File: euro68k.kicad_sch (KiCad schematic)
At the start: 5 parts, among them U1 68000D, U2 AS6C4008-55PCN, U3 28C256, U4 AS6C4008-55PCN, U5 28C256

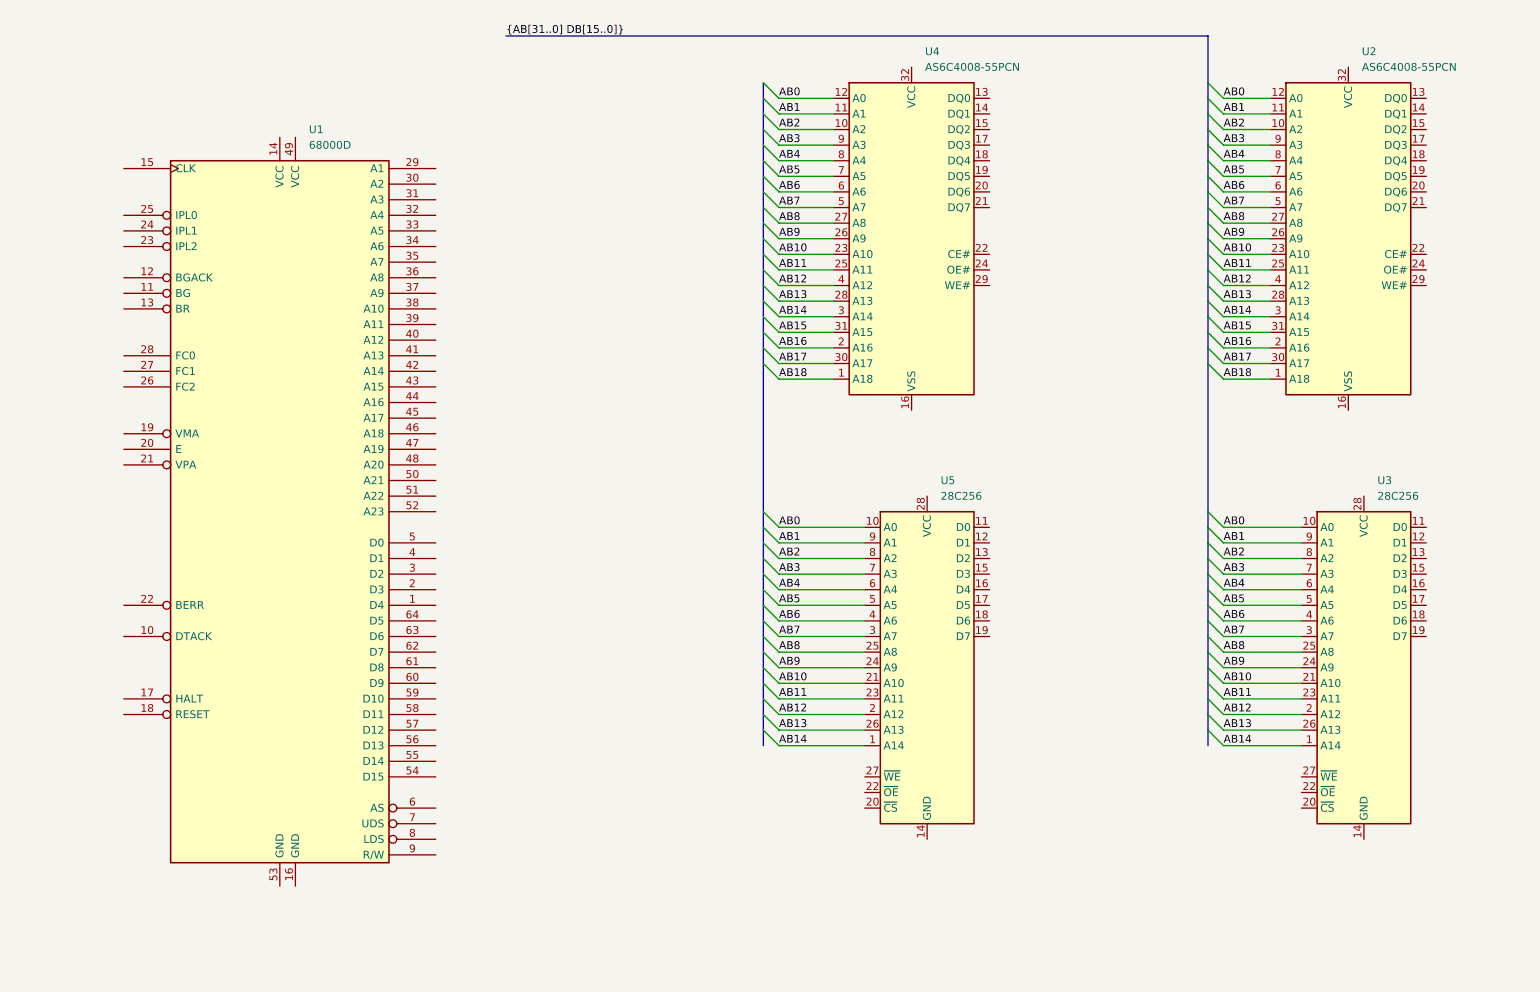
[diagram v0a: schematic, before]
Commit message: databuss til minne
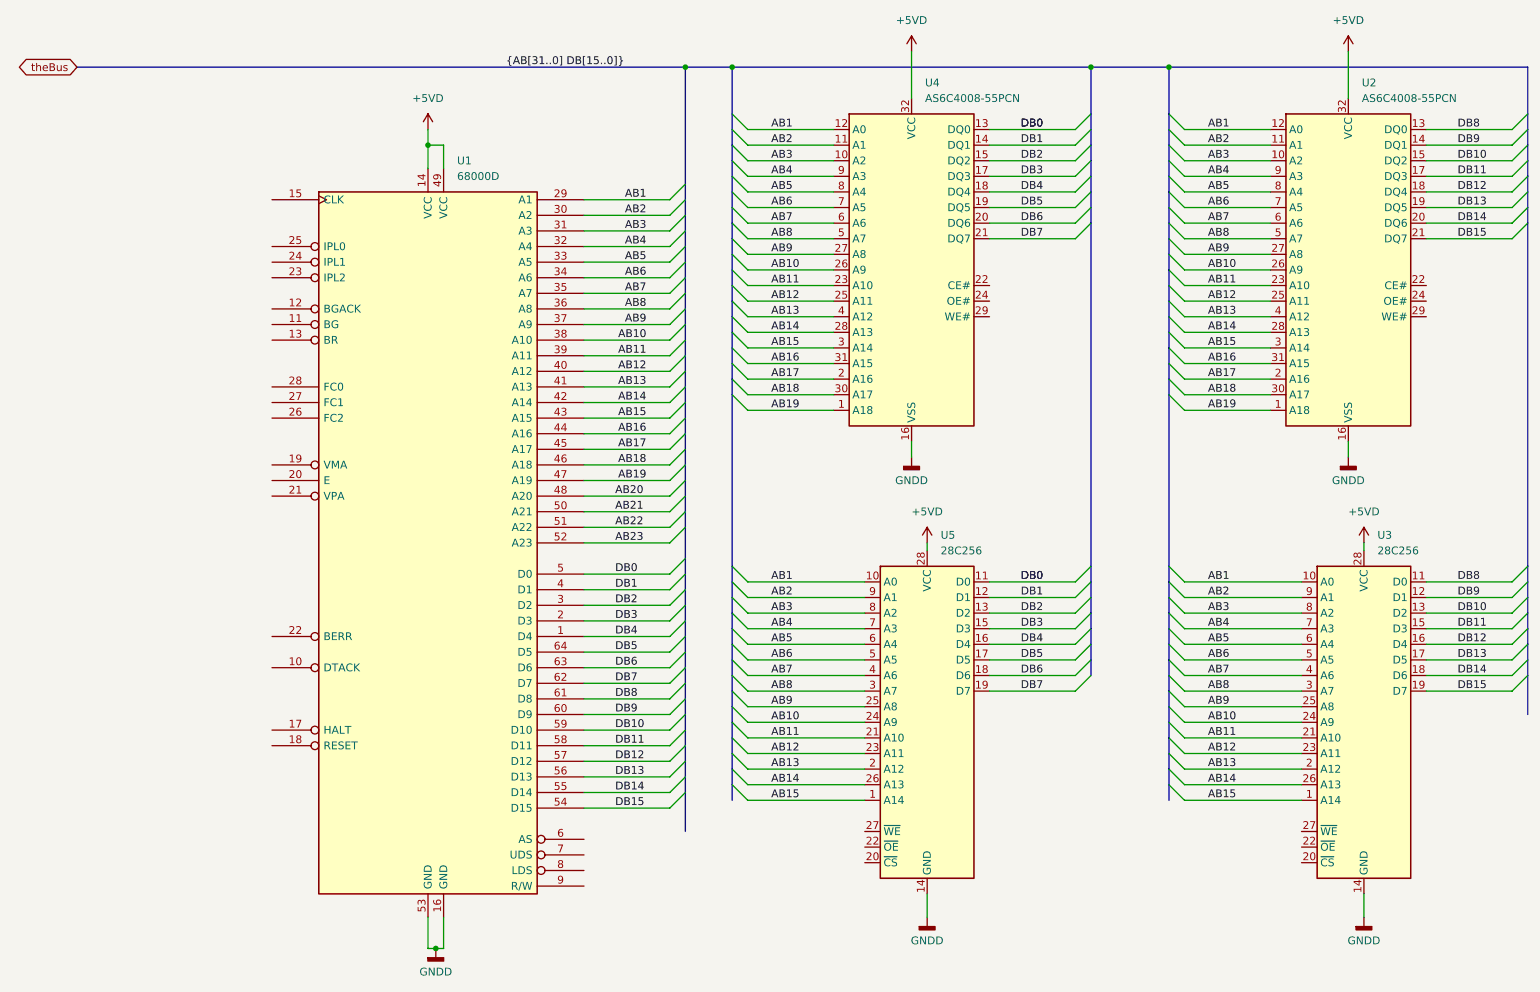
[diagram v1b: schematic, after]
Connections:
- net AB0 is gone; now on net AB1: U2.12 (A0), U3.10 (A0), U4.12 (A0), U5.10 (A0)
- net AB1: now also U1.29 (A1); no longer U2.11 (A1), U3.9 (A1), U4.11 (A1), U5.9 (A1)
- net AB10: now also U1.38 (A10), U2.26 (A9), U3.24 (A9), U4.26 (A9), U5.24 (A9); no longer U2.23 (A10), U3.21 (A10), U4.23 (A10), U5.21 (A10)
- net AB11: now also U1.39 (A11), U2.23 (A10), U3.21 (A10), U4.23 (A10), U5.21 (A10); no longer U2.25 (A11), U3.23 (A11), U4.25 (A11), U5.23 (A11)
- net AB12: now also U1.40 (A12), U2.25 (A11), U3.23 (A11), U4.25 (A11), U5.23 (A11); no longer U2.4 (A12), U3.2 (A12), U4.4 (A12), U5.2 (A12)
- net AB13: now also U1.41 (A13), U2.4 (A12), U3.2 (A12), U4.4 (A12), U5.2 (A12); no longer U2.28 (A13), U3.26 (A13), U4.28 (A13), U5.26 (A13)
- net AB14: now also U1.42 (A14), U2.28 (A13), U3.26 (A13), U4.28 (A13), U5.26 (A13); no longer U2.3 (A14), U3.1 (A14), U4.3 (A14), U5.1 (A14)
- net AB15: now also U1.43 (A15), U2.3 (A14), U3.1 (A14), U4.3 (A14), U5.1 (A14); no longer U2.31 (A15), U4.31 (A15)
- net AB16: now also U1.44 (A16), U2.31 (A15), U4.31 (A15); no longer U2.2 (A16), U4.2 (A16)
- net AB17: now also U1.45 (A17), U2.2 (A16), U4.2 (A16); no longer U2.30 (A17), U4.30 (A17)
- net AB18: now also U1.46 (A18), U2.30 (A17), U4.30 (A17); no longer U2.1 (A18), U4.1 (A18)
- net AB2: now also U1.30 (A2), U2.11 (A1), U3.9 (A1), U4.11 (A1), U5.9 (A1); no longer U2.10 (A2), U3.8 (A2), U4.10 (A2), U5.8 (A2)
- net AB3: now also U1.31 (A3), U2.10 (A2), U3.8 (A2), U4.10 (A2), U5.8 (A2); no longer U2.9 (A3), U3.7 (A3), U4.9 (A3), U5.7 (A3)
- net AB4: now also U1.32 (A4), U2.9 (A3), U3.7 (A3), U4.9 (A3), U5.7 (A3); no longer U2.8 (A4), U3.6 (A4), U4.8 (A4), U5.6 (A4)
- net AB5: now also U1.33 (A5), U2.8 (A4), U3.6 (A4), U4.8 (A4), U5.6 (A4); no longer U2.7 (A5), U3.5 (A5), U4.7 (A5), U5.5 (A5)
- net AB6: now also U1.34 (A6), U2.7 (A5), U3.5 (A5), U4.7 (A5), U5.5 (A5); no longer U2.6 (A6), U3.4 (A6), U4.6 (A6), U5.4 (A6)
- net AB7: now also U1.35 (A7), U2.6 (A6), U3.4 (A6), U4.6 (A6), U5.4 (A6); no longer U2.5 (A7), U3.3 (A7), U4.5 (A7), U5.3 (A7)
- net AB8: now also U1.36 (A8), U2.5 (A7), U3.3 (A7), U4.5 (A7), U5.3 (A7); no longer U2.27 (A8), U3.25 (A8), U4.27 (A8), U5.25 (A8)
- net AB9: now also U1.37 (A9), U2.27 (A8), U3.25 (A8), U4.27 (A8), U5.25 (A8); no longer U2.26 (A9), U3.24 (A9), U4.26 (A9), U5.24 (A9)
- net DB4: now reaches U1.1 (D4)
- net DB4: now also U4.18 (DQ4), U5.16 (D4)
- net +5VD: now reaches U1.14 (VCC)
- net +5VD: now also U1.49 (VCC), U2.32 (VCC), U3.28 (VCC), U4.32 (VCC), U5.28 (VCC)
- net GNDD: now reaches U1.16 (GND)
- net GNDD: now also U1.53 (GND), U2.16 (VSS), U3.14 (GND), U4.16 (VSS), U5.14 (GND)
- net DB3: now reaches U1.2 (D3)
- net DB3: now also U4.17 (DQ3), U5.15 (D3)
- net DB2: now reaches U1.3 (D2)
- net DB2: now also U4.15 (DQ2), U5.13 (D2)
- net DB1: now reaches U1.4 (D1)
- net DB1: now also U4.14 (DQ1), U5.12 (D1)
- net AB19: now reaches U1.47 (A19)
- net AB19: now also U2.1 (A18), U4.1 (A18)
- net AB20: now reaches U1.48 (A20)
- net DB0: now reaches U1.5 (D0)
- net DB0: now also U4.13 (DQ0), U5.11 (D0)
- net AB21: now reaches U1.50 (A21)
- net AB22: now reaches U1.51 (A22)
- net AB23: now reaches U1.52 (A23)
- net DB15: now reaches U1.54 (D15)
- net DB15: now also U2.21 (DQ7), U3.19 (D7)
- net DB14: now reaches U1.55 (D14)
- net DB14: now also U2.20 (DQ6), U3.18 (D6)
- net DB13: now reaches U1.56 (D13)
- net DB13: now also U2.19 (DQ5), U3.17 (D5)
- net DB12: now reaches U1.57 (D12)
- net DB12: now also U2.18 (DQ4), U3.16 (D4)
- net DB11: now reaches U1.58 (D11)
- net DB11: now also U2.17 (DQ3), U3.15 (D3)
- net DB10: now reaches U1.59 (D10)
- net DB10: now also U2.15 (DQ2), U3.13 (D2)
- net DB9: now reaches U1.60 (D9)
- net DB9: now also U2.14 (DQ1), U3.12 (D1)
- net DB8: now reaches U1.61 (D8)
- net DB8: now also U2.13 (DQ0), U3.11 (D0)
- net DB7: now reaches U1.62 (D7)
- net DB7: now also U4.21 (DQ7), U5.19 (D7)
- net DB6: now reaches U1.63 (D6)
- net DB6: now also U4.20 (DQ6), U5.18 (D6)
- net DB5: now reaches U1.64 (D5)
- net DB5: now also U4.19 (DQ5), U5.17 (D5)
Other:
- moved on the sheet: U1, U2, U3, U4, U5
